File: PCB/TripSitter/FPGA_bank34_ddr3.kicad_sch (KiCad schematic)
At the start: 12 parts, among them IC2 MT41J128M16JT-125_K, U1 XC7A100T-FGG484, X1 XO53 100Mhz

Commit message: more pcb routing
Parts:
- removed C16: 100uF, Capacitor_SMD:C_1210_3225Metric_Pad1.33x2.70mm_HandSolder, symbol Device:C_Small
- removed C19: 47uF, Capacitor_SMD:C_1210_3225Metric_Pad1.33x2.70mm_HandSolder, symbol Device:C_Small
- removed C20 (x2): 4.7uF, Capacitor_SMD:C_0805_2012Metric_Pad1.18x1.45mm_HandSolder, symbol Device:C_Small
- removed R804: 100R, Resistor_SMD:R_0201_0603Metric_Pad0.64x0.40mm_HandSolder, symbol Device:R_Small
- added C36: 47uF, Capacitor_SMD:C_1210_3225Metric_Pad1.33x2.70mm_HandSolder, symbol Device:C
- added C37, C38: 4.7uF, Capacitor_SMD:C_0805_2012Metric_Pad1.18x1.45mm_HandSolder, symbol Device:C
- added C80, C81, C82, C83: 470nF, Capacitor_SMD:C_0201_0603Metric_Pad0.64x0.40mm_HandSolder, symbol Device:C
- added R19: 100R, symbol Device:R_Small
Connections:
- net +1V5: now also C36.1, C37.1, C38.1, C80.1, C81.1, C82.1, C83.1
- net DDR3_A0: now also U1.W6 (IO_L15P_T2_DQS_34); no longer U1.AB5 (IO_L10N_T1_34)
- net DDR3_A10: now also U1.T3 (IO_0_34); no longer U1.AB6 (IO_L20N_T3_34)
- net DDR3_A11: now also U1.W5 (IO_L15N_T2_DQS_34); no longer U1.AB7 (IO_L20P_T3_34)
- net DDR3_A13: now also U1.Y2 (IO_L4N_T0_34); no longer U1.AB1 (IO_L7N_T1_34)
- net DDR3_A2: now also U1.Y4 (IO_L11P_T1_SRCC_34); no longer U1.AB3 (IO_L8P_T1_34)
- net DDR3_A3: now also U1.V4 (IO_L12P_T1_MRCC_34); no longer U1.U1 (IO_L1N_T0_34)
- net DDR3_A4: now also U1.V5 (IO_L16N_T2_34); no longer U1.Y9 (IO_L24N_T3_34)
- net DDR3_A5: now also U1.U2 (IO_L2P_T0_34); no longer U1.W1 (IO_L5P_T0_34)
- net DDR3_A6: now also U1.Y3 (IO_L9P_T1_DQS_34); no longer U1.AA8 (IO_L22P_T3_34)
- net DDR3_A7: now also U1.R6 (IO_L17P_T2_34); no longer U1.Y1 (IO_L5N_T0_34)
- net DDR3_A8: now also U1.AA3 (IO_L9N_T1_DQS_34); no longer U1.AB8 (IO_L22N_T3_34)
- net DDR3_A9: now also U1.W2 (IO_L4P_T0_34); no longer U1.AB2 (IO_L8N_T1_34)
- net DDR3_BA0: now also U1.T5 (IO_L14P_T2_SRCC_34); no longer U1.T1 (IO_L1P_T0_34)
- net DDR3_BA1: now also U1.U3 (IO_L6P_T0_34); no longer U1.W9 (IO_L24P_T3_34)
- net DDR3_CK_N: now also U1.V7 (IO_L19P_T3_34), R19.2; no longer U1.V9 (IO_L21P_T3_DQS_34)
- net DDR3_CK_P: now also R19.1
- net DDR3_DQ0: now also U1.AA1 (IO_L7P_T1_34); no longer U1.Y8 (IO_L23P_T3_34)
- net DDR3_DQ1: now also U1.AB5 (IO_L10N_T1_34); no longer U1.V2 (IO_L2N_T0_34)
- net DDR3_DQ10: now also U1.Y9 (IO_L24N_T3_34); no longer U1.V5 (IO_L16N_T2_34)
- net DDR3_DQ11: now also U1.T1 (IO_L1P_T0_34); no longer U1.T5 (IO_L14P_T2_SRCC_34)
- net DDR3_DQ12: now also U1.AB8 (IO_L22N_T3_34); no longer U1.W6 (IO_L15P_T2_DQS_34)
- net DDR3_DQ14: now also U1.Y8 (IO_L23P_T3_34); no longer U1.AA5 (IO_L10P_T1_34)
- net DDR3_DQ15: now also U1.W1 (IO_L5P_T0_34); no longer U1.Y4 (IO_L11P_T1_SRCC_34)
- net DDR3_DQ2: now also U1.R2 (IO_L3N_T0_DQS_34); no longer U1.U2 (IO_L2P_T0_34)
- net DDR3_DQ3: now also U1.W9 (IO_L24P_T3_34); no longer U1.U3 (IO_L6P_T0_34)
- net DDR3_DQ4: now also U1.AB3 (IO_L8P_T1_34); no longer U1.W2 (IO_L4P_T0_34)
- net DDR3_DQ5: now also U1.V9 (IO_L21P_T3_DQS_34); no longer U1.V7 (IO_L19P_T3_34)
- net DDR3_DQ6: now also U1.AA5 (IO_L10P_T1_34); no longer U1.T3 (IO_0_34)
- net DDR3_DQ7: now also U1.R3 (IO_L3P_T0_DQS_34); no longer U1.Y2 (IO_L4N_T0_34)
- net DDR3_DQ8: now also U1.AB7 (IO_L20P_T3_34); no longer U1.W5 (IO_L15N_T2_DQS_34)
- net DDR3_DQ9: now also U1.U1 (IO_L1N_T0_34); no longer U1.V4 (IO_L12P_T1_MRCC_34)
- net DDR3_LDM: now also U1.AB6 (IO_L20N_T3_34); no longer U1.Y7 (IO_L23N_T3_34)
- net DDR3_LDQS_N: now also U1.AB2 (IO_L8N_T1_34); no longer U1.R2 (IO_L3N_T0_DQS_34)
- net DDR3_LDQS_P: now also U1.AB1 (IO_L7N_T1_34); no longer U1.R3 (IO_L3P_T0_DQS_34)
- net DDR3_UDM: now also U1.Y1 (IO_L5N_T0_34); no longer U1.R6 (IO_L17P_T2_34)
- net DDR3_UDQS_N: now also U1.Y7 (IO_L23N_T3_34); no longer U1.Y3 (IO_L9P_T1_DQS_34)
- net DDR3_UDQS_P: now also U1.AA8 (IO_L22P_T3_34); no longer U1.AA3 (IO_L9N_T1_DQS_34)
- net DDR3_nRESET: now also U1.V2 (IO_L2N_T0_34); no longer U1.AA1 (IO_L7P_T1_34)
- net GND: now also C36.2, C37.2, C38.2, C80.2, C81.2, C82.2, C83.2
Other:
- moved on the sheet: U1H, X1

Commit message: pcb: Finalized routing without DDR3
Added ground and power plane, layed out all the components, fanned out
BGA. QSPI between FPGA->MCU->SRAM and MCU->SRAM is routed. Most is done
but DRC does not pass so do not produce.
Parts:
- removed C36: 47uF, Capacitor_SMD:C_1210_3225Metric_Pad1.33x2.70mm_HandSolder, symbol Device:C
- removed C37, C38: 4.7uF, Capacitor_SMD:C_0805_2012Metric_Pad1.18x1.45mm_HandSolder, symbol Device:C
- removed C80, C81, C82, C83: 470nF, Capacitor_SMD:C_0201_0603Metric_Pad0.64x0.40mm_HandSolder, symbol Device:C
- removed C94, C95: 0.1uF, Capacitor_SMD:C_0201_0603Metric_Pad0.64x0.40mm_HandSolder, symbol Device:C_Small
- removed C96: 100uF, Capacitor_SMD:C_0805_2012Metric_Pad1.18x1.45mm_HandSolder, symbol Device:C_Small
- removed IC2: MT41J128M16JT-125_K, Package_BGA:Micron_FBGA-96_8x14mm_Layout9x16_P0.8mm, symbol MT41J128M16JT:MT41J128M16JT-125_K
- removed R13: 240, Resistor_SMD:R_0805_2012Metric_Pad1.20x1.40mm_HandSolder, symbol Device:R_Small
- removed R19: 100R, symbol Device:R_Small
- removed X1: XO53 100Mhz, Oscillator:Oscillator_SMD_EuroQuartz_XO53-4Pin_5.0x3.2mm_HandSoldering, symbol Oscillator:XO32
- added unit 3 of U1
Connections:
- removed net +1V5: U1.AA7 (VCCO_34), U1.AB4 (VCCO_34), U1.R5 (VCCO_34), U1.T2 (VCCO_34), U1.V6 (VCCO_34), U1.W3 (VCCO_34)
- net DDR3_A0: no longer names the net of U1.W6 (IO_L15P_T2_DQS_34)
- net DDR3_A1: no longer names the net of U1.Y6 (IO_L18P_T2_34)
- net DDR3_A10: no longer names the net of U1.T3 (IO_0_34)
- net DDR3_A11: no longer names the net of U1.W5 (IO_L15N_T2_DQS_34)
- net DDR3_A12: no longer names the net of U1.AA6 (IO_L18N_T2_34)
- net DDR3_A13: no longer names the net of U1.Y2 (IO_L4N_T0_34)
- net DDR3_A2: no longer names the net of U1.Y4 (IO_L11P_T1_SRCC_34)
- net DDR3_A3: no longer names the net of U1.V4 (IO_L12P_T1_MRCC_34)
- net DDR3_A4: no longer names the net of U1.V5 (IO_L16N_T2_34)
- net DDR3_A5: no longer names the net of U1.U2 (IO_L2P_T0_34)
- net DDR3_A6: no longer names the net of U1.Y3 (IO_L9P_T1_DQS_34)
- net DDR3_A7: no longer names the net of U1.R6 (IO_L17P_T2_34)
- net DDR3_A8: no longer names the net of U1.AA3 (IO_L9N_T1_DQS_34)
- net DDR3_A9: no longer names the net of U1.W2 (IO_L4P_T0_34)
- net DDR3_BA0: no longer names the net of U1.T5 (IO_L14P_T2_SRCC_34)
- net DDR3_BA1: no longer names the net of U1.U3 (IO_L6P_T0_34)
- net DDR3_BA2: no longer names the net of U1.AA4 (IO_L11N_T1_SRCC_34)
- net DDR3_CKE: no longer names the net of U1.R4 (IO_L13P_T2_MRCC_34)
- net DDR3_CK_N: no longer names the net of U1.V7 (IO_L19P_T3_34)
- net DDR3_CK_P: no longer names the net of U1.V8 (IO_L21N_T3_DQS_34)
- net DDR3_DQ0: no longer names the net of U1.AA1 (IO_L7P_T1_34)
- net DDR3_DQ1: no longer names the net of U1.AB5 (IO_L10N_T1_34)
- net DDR3_DQ10: no longer names the net of U1.Y9 (IO_L24N_T3_34)
- net DDR3_DQ11: no longer names the net of U1.T1 (IO_L1P_T0_34)
- net DDR3_DQ12: no longer names the net of U1.AB8 (IO_L22N_T3_34)
- net DDR3_DQ13: no longer names the net of U1.W7 (IO_L19N_T3_VREF_34)
- net DDR3_DQ14: no longer names the net of U1.Y8 (IO_L23P_T3_34)
- net DDR3_DQ15: no longer names the net of U1.W1 (IO_L5P_T0_34)
- net DDR3_DQ2: no longer names the net of U1.R2 (IO_L3N_T0_DQS_34)
- net DDR3_DQ3: no longer names the net of U1.W9 (IO_L24P_T3_34)
- net DDR3_DQ4: no longer names the net of U1.AB3 (IO_L8P_T1_34)
- net DDR3_DQ5: no longer names the net of U1.V9 (IO_L21P_T3_DQS_34)
- net DDR3_DQ6: no longer names the net of U1.AA5 (IO_L10P_T1_34)
- net DDR3_DQ7: no longer names the net of U1.R3 (IO_L3P_T0_DQS_34)
- net DDR3_DQ8: no longer names the net of U1.AB7 (IO_L20P_T3_34)
- net DDR3_DQ9: no longer names the net of U1.U1 (IO_L1N_T0_34)
- net DDR3_LDM: no longer names the net of U1.AB6 (IO_L20N_T3_34)
- net DDR3_LDQS_N: no longer names the net of U1.AB2 (IO_L8N_T1_34)
- net DDR3_LDQS_P: no longer names the net of U1.AB1 (IO_L7N_T1_34)
- net DDR3_ODT: no longer names the net of U1.T6 (IO_L17N_T2_34)
- net DDR3_UDM: no longer names the net of U1.Y1 (IO_L5N_T0_34)
- net DDR3_UDQS_N: no longer names the net of U1.Y7 (IO_L23N_T3_34)
- net DDR3_UDQS_P: no longer names the net of U1.AA8 (IO_L22P_T3_34)
- net DDR3_nCAS: no longer names the net of U1.U6 (IO_L16P_T2_34)
- net DDR3_nCS: no longer names the net of U1.U7 (IO_25_34)
- net DDR3_nRAS: no longer names the net of U1.U5 (IO_L14N_T2_SRCC_34)
- net DDR3_nRESET: no longer names the net of U1.V2 (IO_L2N_T0_34)
- net DDR3_nWE: no longer names the net of U1.T4 (IO_L13N_T2_MRCC_34)
- net XO_Enable: no longer names the net of U1.V3 (IO_L6N_T0_VREF_34)
- no-connect marks 9 -> 112
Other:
- note added: "UNUSED wasn't able to route out DDR3"
- note removed: "We don't need to route A14 for 2GB"

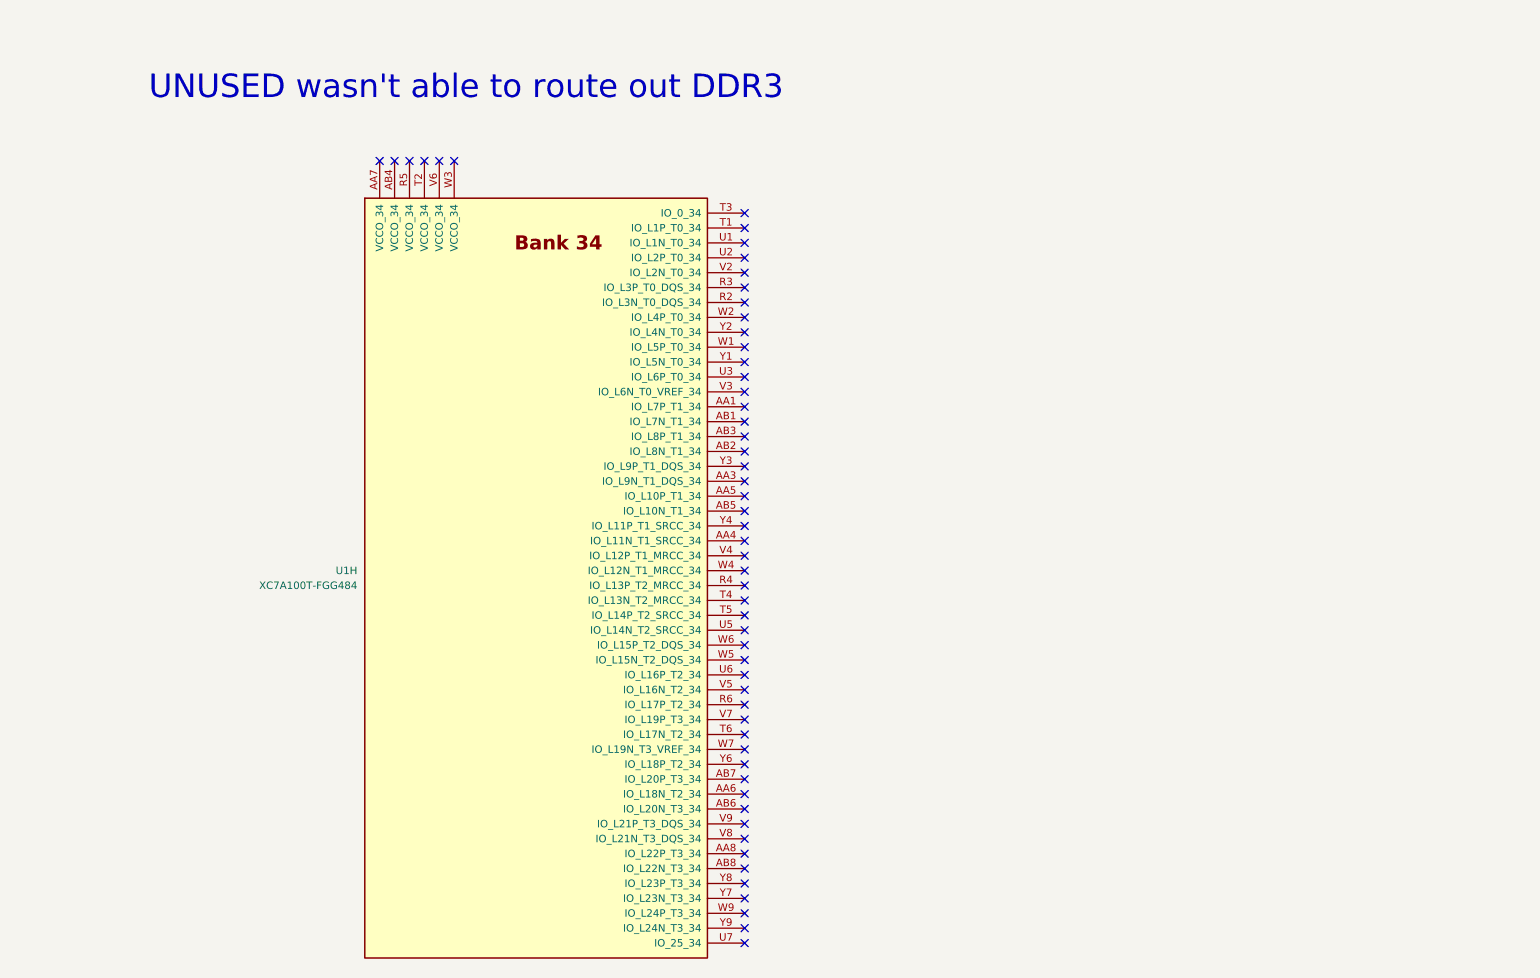
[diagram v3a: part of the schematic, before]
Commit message: route 2 separate QSPI buses to SRAM from FPGA
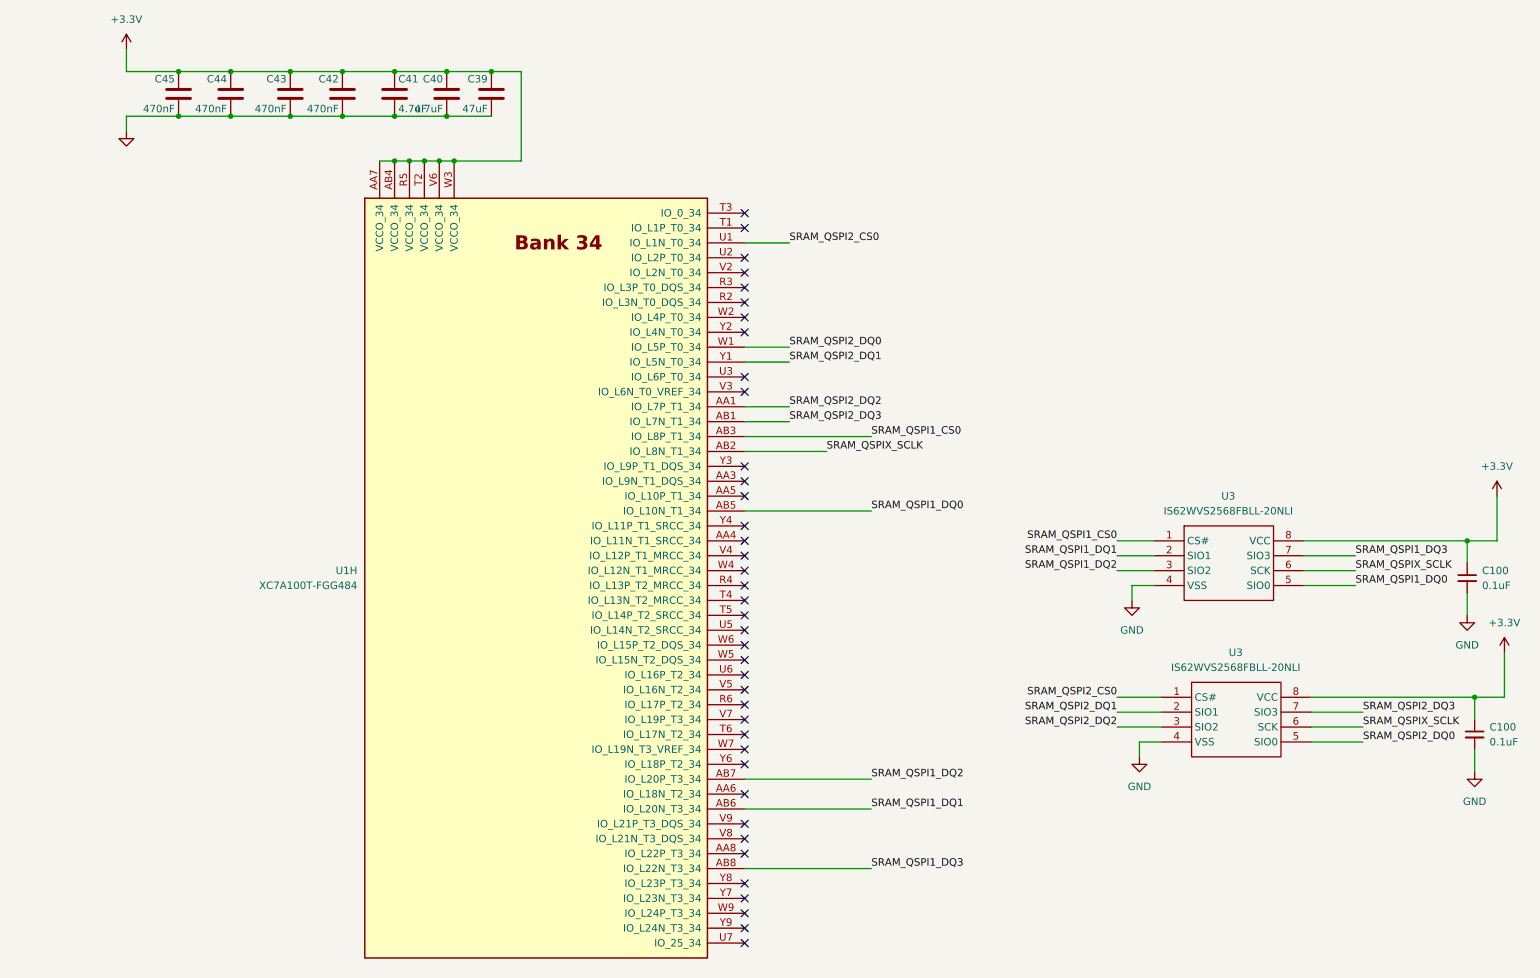
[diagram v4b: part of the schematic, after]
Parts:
- added C100 (x2): 0.1uF, Capacitor_SMD:C_0201_0603Metric_Pad0.64x0.40mm_HandSolder, symbol Device:C_Small
- added C39: 47uF, Capacitor_SMD:C_1210_3225Metric_Pad1.33x2.70mm_HandSolder, symbol Device:C
- added C40, C41: 4.7uF, Capacitor_SMD:C_0805_2012Metric_Pad1.18x1.45mm_HandSolder, symbol Device:C
- added C42, C43, C44, C45: 470nF, Capacitor_SMD:C_0201_0603Metric_Pad0.64x0.40mm_HandSolder, symbol Device:C
- added U3 (x2): IS62WVS2568FBLL-20NLI, Package_SO:SOIC-8_3.9x4.9mm_P1.27mm, symbol 0000_CustomComponents:IS62WVS2568FBLL-20NLI-TR | SQI Mode
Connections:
- net SRAM_QSPI2_DQ2: now reaches U1.AA1 (IO_L7P_T1_34)
- net SRAM_QSPI2_DQ2: now also U3.3 (SIO2)
- net +3.3V: now reaches U1.AA7 (VCCO_34)
- net +3.3V: now also U1.AB4 (VCCO_34), U1.R5 (VCCO_34), U1.T2 (VCCO_34), U1.V6 (VCCO_34), U1.W3 (VCCO_34), C100.1, C100.1, C39.1, C40.1, C41.1, C42.1, C43.1, C44.1, C45.1, U3.8 (VCC), U3.8 (VCC)
- net SRAM_QSPI2_DQ3: now reaches U1.AB1 (IO_L7N_T1_34)
- net SRAM_QSPI2_DQ3: now also U3.7 (SIO3)
- net SRAM_QSPIX_SCLK: now reaches U1.AB2 (IO_L8N_T1_34)
- net SRAM_QSPIX_SCLK: now also U3.6 (SCK), U3.6 (SCK)
- net SRAM_QSPI1_CS0: now reaches U1.AB3 (IO_L8P_T1_34)
- net SRAM_QSPI1_CS0: now also U3.1 (CS#)
- net SRAM_QSPI1_DQ0: now reaches U1.AB5 (IO_L10N_T1_34)
- net SRAM_QSPI1_DQ0: now also U3.5 (SIO0)
- net SRAM_QSPI1_DQ1: now reaches U1.AB6 (IO_L20N_T3_34)
- net SRAM_QSPI1_DQ1: now also U3.2 (SIO1)
- net SRAM_QSPI1_DQ2: now reaches U1.AB7 (IO_L20P_T3_34)
- net SRAM_QSPI1_DQ2: now also U3.3 (SIO2)
- net SRAM_QSPI1_DQ3: now reaches U1.AB8 (IO_L22N_T3_34)
- net SRAM_QSPI1_DQ3: now also U3.7 (SIO3)
- net SRAM_QSPI2_CS0: now reaches U1.U1 (IO_L1N_T0_34)
- net SRAM_QSPI2_CS0: now also U3.1 (CS#)
- net SRAM_QSPI2_DQ0: now reaches U1.W1 (IO_L5P_T0_34)
- net SRAM_QSPI2_DQ0: now also U3.5 (SIO0)
- net SRAM_QSPI2_DQ1: now reaches U1.Y1 (IO_L5N_T0_34)
- net SRAM_QSPI2_DQ1: now also U3.2 (SIO1)
- new net GND: C100.2, C100.2, C39.2, C40.2, C41.2, C42.2, C43.2, C44.2, C45.2, U3.4 (VSS), U3.4 (VSS)
- no-connect marks 112 -> 95
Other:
- note removed: "UNUSED wasn't able to route out DDR3"
